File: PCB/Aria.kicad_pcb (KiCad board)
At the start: 4 copper layers, 30 x 85 mm, 85 parts, among them J1 B2B-PH-K-S(LF)(SN), J2 B3B-PH-K-S(LF)(SN), J3 20021121-00010C4LF, J4 0475890001-MicroUSBPort, P1 CONN_01X20, P2 CONN_01X20, Q1 DMG2307L-7, Q2 DMG2307L-7, SW1 B3U-1000P, SW2 B3U-1000P, T1 1909763-1, U1 BQ24210DQCT, U2 AZ1117CR-3.3TRG1_1, U3 STM32F446RET6_-_TQFP64, U4 ESP8285, X1 ABM3B8.000MHZB2T, X2 ABS07-32.768KHZ-9-T, X3 FA-128_26.0000MF10Z-AC3

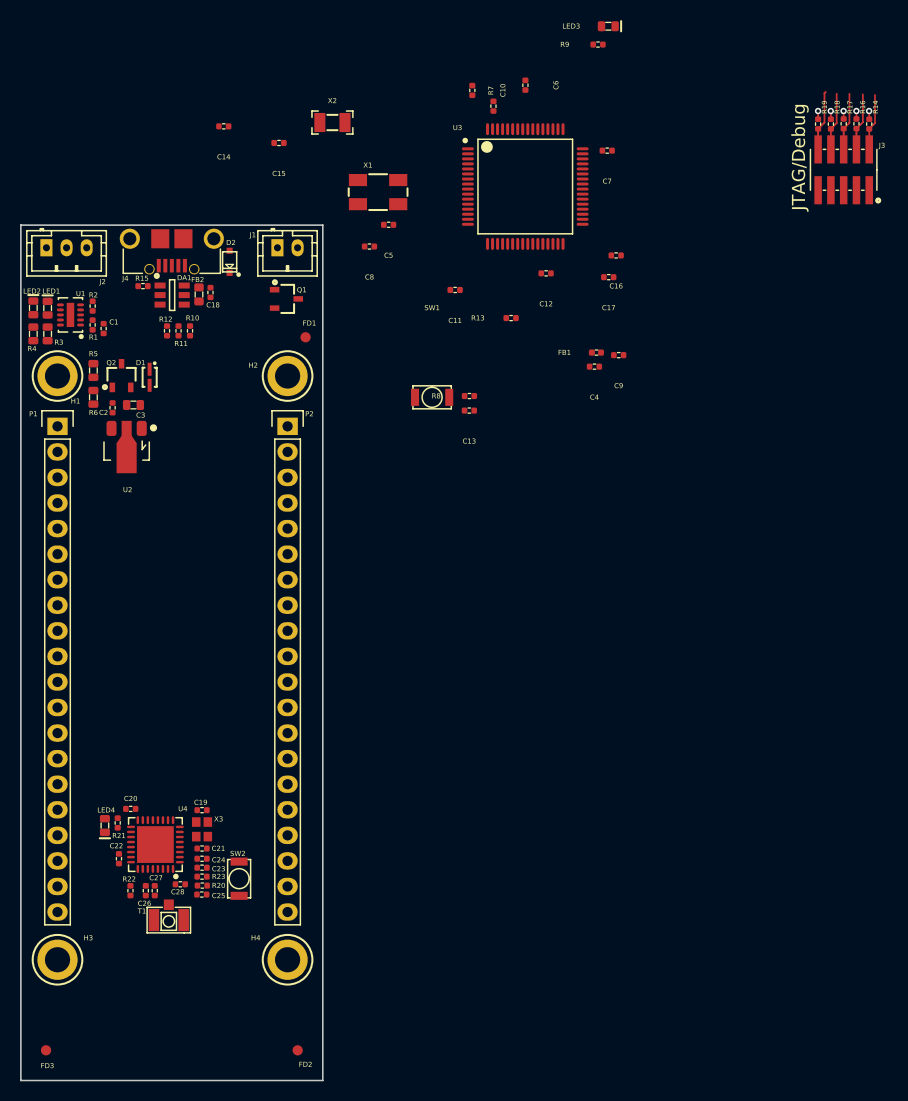
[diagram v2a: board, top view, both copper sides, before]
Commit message: Finished Placement and Mapping
Components placed, some routing completed. pin header mapping figured
out.
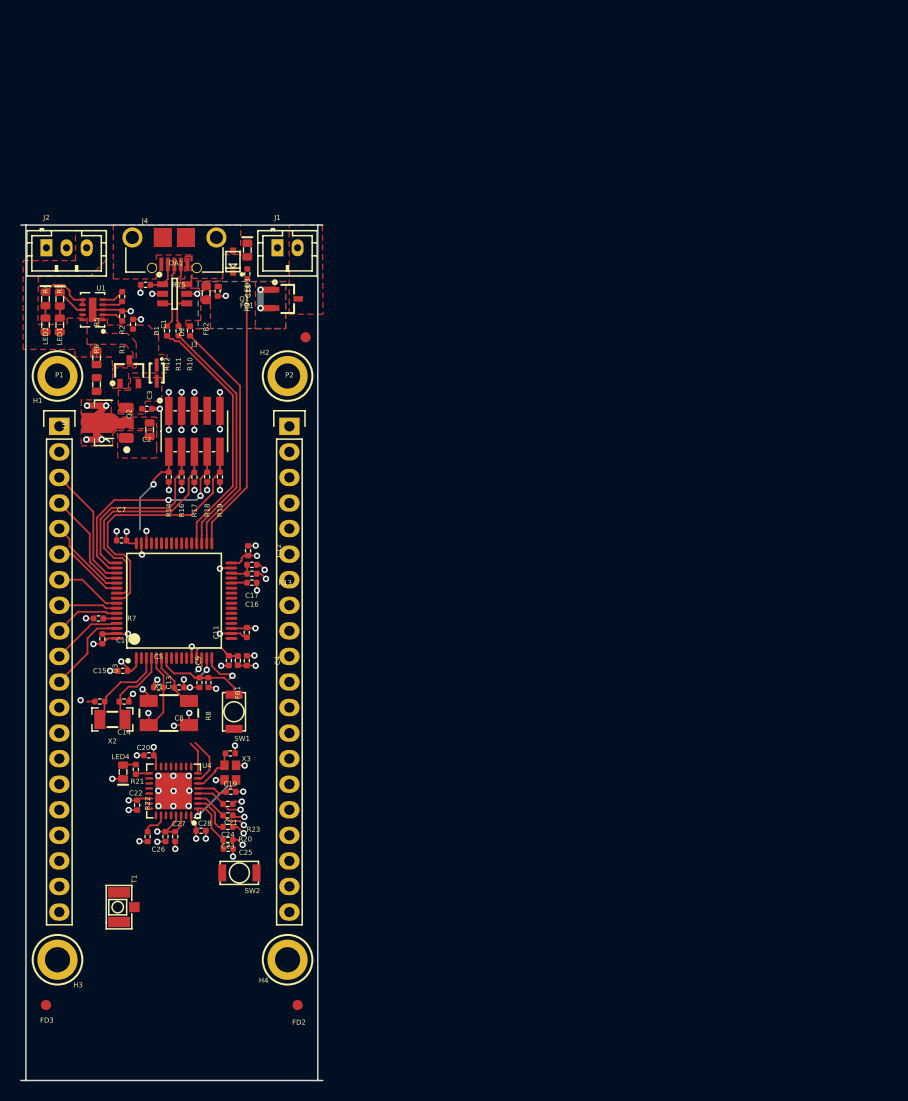
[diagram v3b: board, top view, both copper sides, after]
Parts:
- moved R14 77.9 mm to (68.2, 55.0), turned to 90 degrees
- moved R16 75.7 mm to (69.5, 55.1), turned to 90 degrees
- moved R17 73.5 mm to (70.7, 55.1), turned to 90 degrees
- moved R18 71.2 mm to (72.0, 55.0), turned to 90 degrees
- moved J3 69.5 mm to (70.7, 50.5), turned to 180 degrees
- moved C6 69.2 mm to (61.6, 71.1)
- moved R19 69.0 mm to (73.3, 55.0), turned to 90 degrees
- moved C10 67.3 mm to (63.6, 74.3), turned to 180 degrees
- moved R7 64.3 mm to (61.2, 69.1), turned to 180 degrees
- moved X2 63.2 mm to (62.6, 79.1), turned to 180 degrees
- moved C7 61.9 mm to (63.5, 61.3), turned to 180 degrees
- moved C15 58.3 mm to (61.3, 77.3), turned to 180 degrees
- moved C14 58.0 mm to (63.8, 77.3)
- moved X1 55.8 mm to (68.2, 78.5)
- moved U3 54.0 mm to (68.7, 67.3), turned to 90 degrees
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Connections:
- net Net-(U3-Pad20) renamed /MCU_STM32F446RET6/PA4
- C1 pad 1: /Power/VBUS -> /MCU_STM32F446RET6/VBUS
- C25 pad 1: /WiFi-ESP8285/STM_ESP_RST -> /MCU_STM32F446RET6/STM_ESP_RST
- D1 pad 1: /Power/VBUS -> /MCU_STM32F446RET6/VBUS
- P1 pad 10: Net-(P1-Pad10) -> /MCU_STM32F446RET6/PB8
- P1 pad 11: Net-(P1-Pad11) -> /MCU_STM32F446RET6/PB9
- P1 pad 12: Net-(P1-Pad12) -> /MCU_STM32F446RET6/PC0
- P1 pad 13: Net-(P1-Pad13) -> /MCU_STM32F446RET6/PC1
- P1 pad 14: Net-(P1-Pad14) -> /MCU_STM32F446RET6/PC3
- P1 pad 15: Net-(P1-Pad15) -> /MCU_STM32F446RET6/PC13
- P1 pad 16: Net-(P1-Pad16) -> /MCU_STM32F446RET6/PB0
- P1 pad 17: Net-(P1-Pad17) -> /MCU_STM32F446RET6/PB1
- P1 pad 18: Net-(P1-Pad18) -> GND
- P1 pad 19: Net-(P1-Pad19) -> +3V3
- P1 pad 3: Net-(P1-Pad3) -> /MCU_STM32F446RET6/PC10
- P1 pad 4: Net-(P1-Pad4) -> /MCU_STM32F446RET6/PC11
- P1 pad 5: Net-(P1-Pad5) -> /MCU_STM32F446RET6/PC12
- P1 pad 6: Net-(P1-Pad6) -> /MCU_STM32F446RET6/ESPTOST_BOOT0
- P1 pad 7: Net-(P1-Pad7) -> /MCU_STM32F446RET6/PB5
- P1 pad 8: Net-(P1-Pad8) -> /MCU_STM32F446RET6/PB6
- P1 pad 9: Net-(P1-Pad9) -> /MCU_STM32F446RET6/PB7
- P2 pad 10: Net-(P2-Pad10) -> /MCU_STM32F446RET6/PC6
- P2 pad 11: Net-(P2-Pad11) -> /MCU_STM32F446RET6/PC7
- P2 pad 12: Net-(P2-Pad12) -> /MCU_STM32F446RET6/PB10
- P2 pad 13: Net-(P2-Pad13) -> /MCU_STM32F446RET6/PC5
- P2 pad 14: Net-(P2-Pad14) -> /MCU_STM32F446RET6/PC4
- P2 pad 15: Net-(P2-Pad15) -> /MCU_STM32F446RET6/PA7
- P2 pad 16: Net-(P2-Pad16) -> /MCU_STM32F446RET6/PA6
- P2 pad 17: Net-(P2-Pad17) -> /MCU_STM32F446RET6/PA5
- P2 pad 18: Net-(P2-Pad18) -> GND
- P2 pad 19: Net-(P2-Pad19) -> +3V3
- P2 pad 3: Net-(P2-Pad3) -> /MCU_STM32F446RET6/PA8
- P2 pad 4: Net-(P2-Pad4) -> /MCU_STM32F446RET6/PA9
- P2 pad 5: Net-(P2-Pad5) -> /MCU_STM32F446RET6/PA10
- P2 pad 6: Net-(P2-Pad6) -> /MCU_STM32F446RET6/PA11
- P2 pad 7: Net-(P2-Pad7) -> /MCU_STM32F446RET6/PA12
- P2 pad 8: Net-(P2-Pad8) -> /MCU_STM32F446RET6/PC8
- P2 pad 9: Net-(P2-Pad9) -> /MCU_STM32F446RET6/PC9
- Q1 pad 1: /Power/VBUS -> /MCU_STM32F446RET6/VBUS
- Q1 pad 2: /Power/VBUS -> /MCU_STM32F446RET6/VBUS
- Q2 pad 1: /Power/VBUS -> /MCU_STM32F446RET6/VBUS
- R20 pad 1: /WiFi-ESP8285/STM_ESP_RST -> /MCU_STM32F446RET6/STM_ESP_RST
- R5 pad 2: /Power/BAT_VOLT -> /MCU_STM32F446RET6/BAT_VOLT
- R6 pad 1: /Power/BAT_VOLT -> /MCU_STM32F446RET6/BAT_VOLT
- R7 pad 1: /MCU_STM32F446RET6/ESPTOST_BOOT0 -> Net-(R7-Pad1)
- SW1 pad 1: /MCU_STM32F446RET6/ESP_ST_RST -> Net-(SW1-Pad1)
- SW2 pad 2: /WiFi-ESP8285/STM_ESP_RST -> /MCU_STM32F446RET6/STM_ESP_RST
- U1 pad 1: /Power/VBUS -> /MCU_STM32F446RET6/VBUS
- U3 pad 11: Net-(U3-Pad11) -> /MCU_STM32F446RET6/PC3
- U3 pad 14: Net-(U3-Pad14) -> /MCU_STM32F446RET6/ESP_URX
- U3 pad 15: Net-(U3-Pad15) -> /MCU_STM32F446RET6/ESP_UTX
- U3 pad 16: Net-(U3-Pad16) -> /MCU_STM32F446RET6/STM_ESP_RST
- U3 pad 17: Net-(U3-Pad17) -> /MCU_STM32F446RET6/ESP_PGM_MODE
- U3 pad 2: Net-(U3-Pad2) -> /MCU_STM32F446RET6/PC13
- U3 pad 21: Net-(U3-Pad21) -> /MCU_STM32F446RET6/PA5
- U3 pad 22: Net-(U3-Pad22) -> /MCU_STM32F446RET6/PA6
- U3 pad 23: Net-(U3-Pad23) -> /MCU_STM32F446RET6/PA7
- U3 pad 24: Net-(U3-Pad24) -> /MCU_STM32F446RET6/PC4
- U3 pad 25: Net-(U3-Pad25) -> /MCU_STM32F446RET6/PC5
- U3 pad 26: Net-(U3-Pad26) -> /MCU_STM32F446RET6/PB0
- U3 pad 27: Net-(U3-Pad27) -> /MCU_STM32F446RET6/PB1
- U3 pad 29: Net-(U3-Pad29) -> /MCU_STM32F446RET6/PB10
- U3 pad 37: Net-(U3-Pad37) -> /MCU_STM32F446RET6/PC6
- U3 pad 38: Net-(U3-Pad38) -> /MCU_STM32F446RET6/PC7
- U3 pad 39: Net-(U3-Pad39) -> /MCU_STM32F446RET6/PC8
- U3 pad 40: Net-(U3-Pad40) -> /MCU_STM32F446RET6/PC9
- U3 pad 41: Net-(U3-Pad41) -> /MCU_STM32F446RET6/PA8
- U3 pad 42: Net-(U3-Pad42) -> /MCU_STM32F446RET6/PA9
- U3 pad 43: Net-(U3-Pad43) -> /MCU_STM32F446RET6/PA10
- U3 pad 44: Net-(U3-Pad44) -> /MCU_STM32F446RET6/PA11
- U3 pad 45: Net-(U3-Pad45) -> /MCU_STM32F446RET6/PA12
- U3 pad 51: /MCU_STM32F446RET6/ESP_UTX -> /MCU_STM32F446RET6/PC10
- U3 pad 52: /MCU_STM32F446RET6/ESP_URX -> /MCU_STM32F446RET6/PC11
- U3 pad 53: /MCU_STM32F446RET6/STM_ESP_RST -> /MCU_STM32F446RET6/PC12
- U3 pad 54: /MCU_STM32F446RET6/ESP_PGM_MODE -> /MCU_STM32F446RET6/ESPTOST_BOOT0
- U3 pad 57: Net-(U3-Pad57) -> /MCU_STM32F446RET6/PB5
- U3 pad 58: Net-(U3-Pad58) -> /MCU_STM32F446RET6/PB6
- U3 pad 59: Net-(U3-Pad59) -> /MCU_STM32F446RET6/PB7
- U3 pad 60: /MCU_STM32F446RET6/ESPTOST_BOOT0 -> Net-(R7-Pad1)
- U3 pad 61: Net-(U3-Pad61) -> /MCU_STM32F446RET6/PB8
- U3 pad 62: Net-(U3-Pad62) -> /MCU_STM32F446RET6/PB9
- U3 pad 8: Net-(U3-Pad8) -> /MCU_STM32F446RET6/PC0
- U3 pad 9: Net-(U3-Pad9) -> /MCU_STM32F446RET6/PC1
- U4 pad 22: /WiFi-ESP8285/ESPTOST_BOOT1 -> /MCU_STM32F446RET6/ESPTOST_BOOT1
- U4 pad 23: /WiFi-ESP8285/ESPTOST_BOOT0 -> /MCU_STM32F446RET6/ESPTOST_BOOT0
- U4 pad 24: /WiFi-ESP8285/ESP_ST_RST -> /MCU_STM32F446RET6/ESP_ST_RST
- U4 pad 25: /WiFi-ESP8285/ESP_UTX -> /MCU_STM32F446RET6/ESP_UTX
- U4 pad 26: /WiFi-ESP8285/ESP_URX -> /MCU_STM32F446RET6/ESP_URX
- U4 pad 32: /WiFi-ESP8285/STM_ESP_RST -> /MCU_STM32F446RET6/STM_ESP_RST
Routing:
- net GND: track 0.00 -> 92.4 mm, vias 0 -> 56
- net +3V3: track 4.03 -> 57.0 mm, vias 5 -> 27
- net /MCU_STM32F446RET6/HEARTBEAT: track 0.00 -> 27.8 mm
- net Net-(R12-Pad1): track 0.00 -> 25.2 mm
- net Net-(R11-Pad1): track 0.00 -> 24.4 mm
- net Net-(R10-Pad1): track 0.00 -> 24.1 mm
- net /MCU_STM32F446RET6/NJTRST: track 6.03 -> 26.0 mm
- net /MCU_STM32F446RET6/SWO_TDO: track 5.76 -> 23.4 mm
- net /MCU_STM32F446RET6/SWO_TDI: track 5.76 -> 22.2 mm, vias 0 -> 2
- net /MCU_STM32F446RET6/STM_ESP_RST: track 0.00 -> 14.2 mm, vias 0 -> 2
- net /MCU_STM32F446RET6/SWCLK_TCK: track 5.73 -> 18.9 mm
- net /MCU_STM32F446RET6/PC10: track 0.00 -> 12.6 mm
- net /MCU_STM32F446RET6/PC11: track 0.00 -> 10.6 mm
- net /MCU_STM32F446RET6/ESP_ST_RST: track 0.00 -> 9.27 mm
- net /MCU_STM32F446RET6/PB9: track 0.00 -> 8.98 mm
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- added copper zone on F.Cu, net +3V3
- added copper zone on F.Cu, net /Power/BAT
- added copper zone on B.Cu, net /Power/VBUS
- added copper zone on F.Cu, net /Power/VBUS
- added copper zone on F.Cu, net GND
- added copper zone on F.Cu, net Net-(C18-Pad2)
- added copper zone on F.Cu, net Net-(C2-Pad1)
- added copper zone on F.Cu, net Net-(D2-Pad1)
- added copper zone on F.Cu, net Net-(J1-Pad2)
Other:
- outline, holes or cut-outs redrawn
- board text removed: "JTAG/Debug"

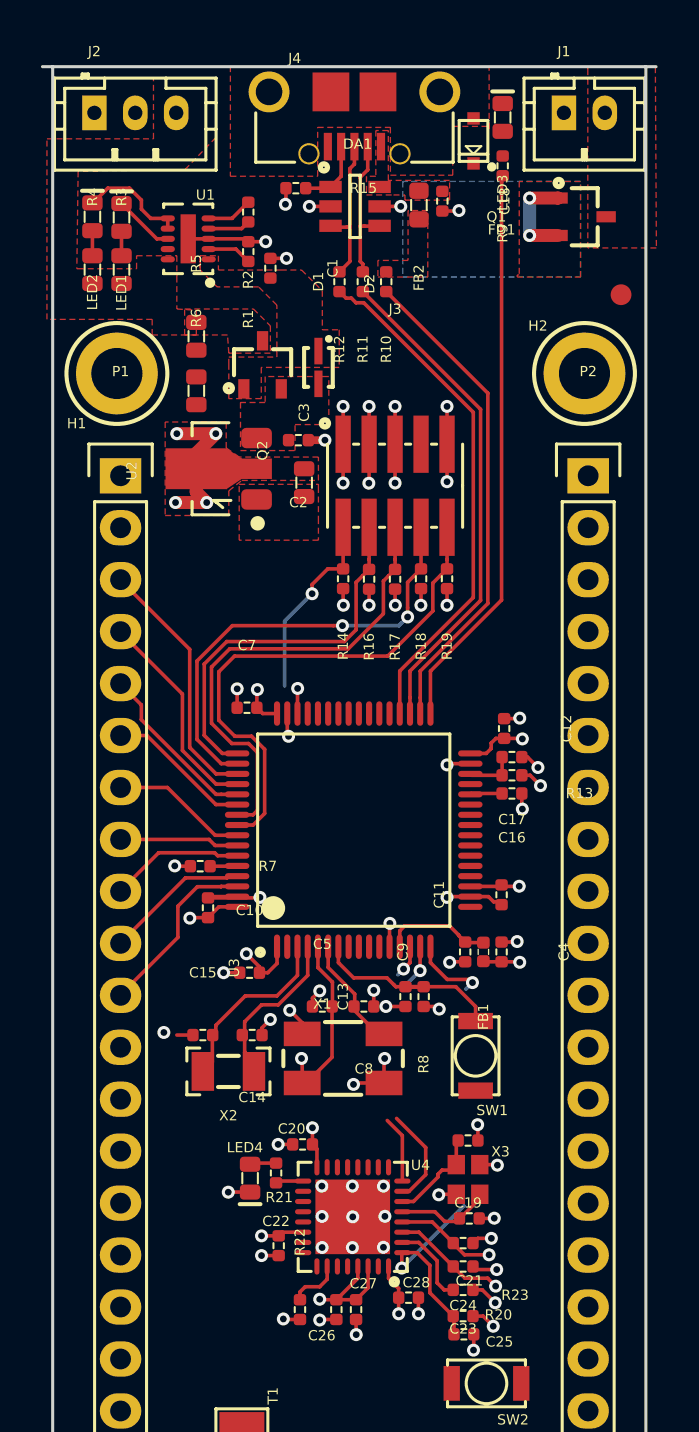
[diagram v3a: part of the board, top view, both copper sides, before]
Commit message: Layout
layout underway, one side completely routed, next other side, ESP, and
PCB antenna. Added PDF for app not on 2.4GHZ antenna similar to the one
sparkfun uses in their thing boards, I suspect this is where they got it
and it seems reliable.
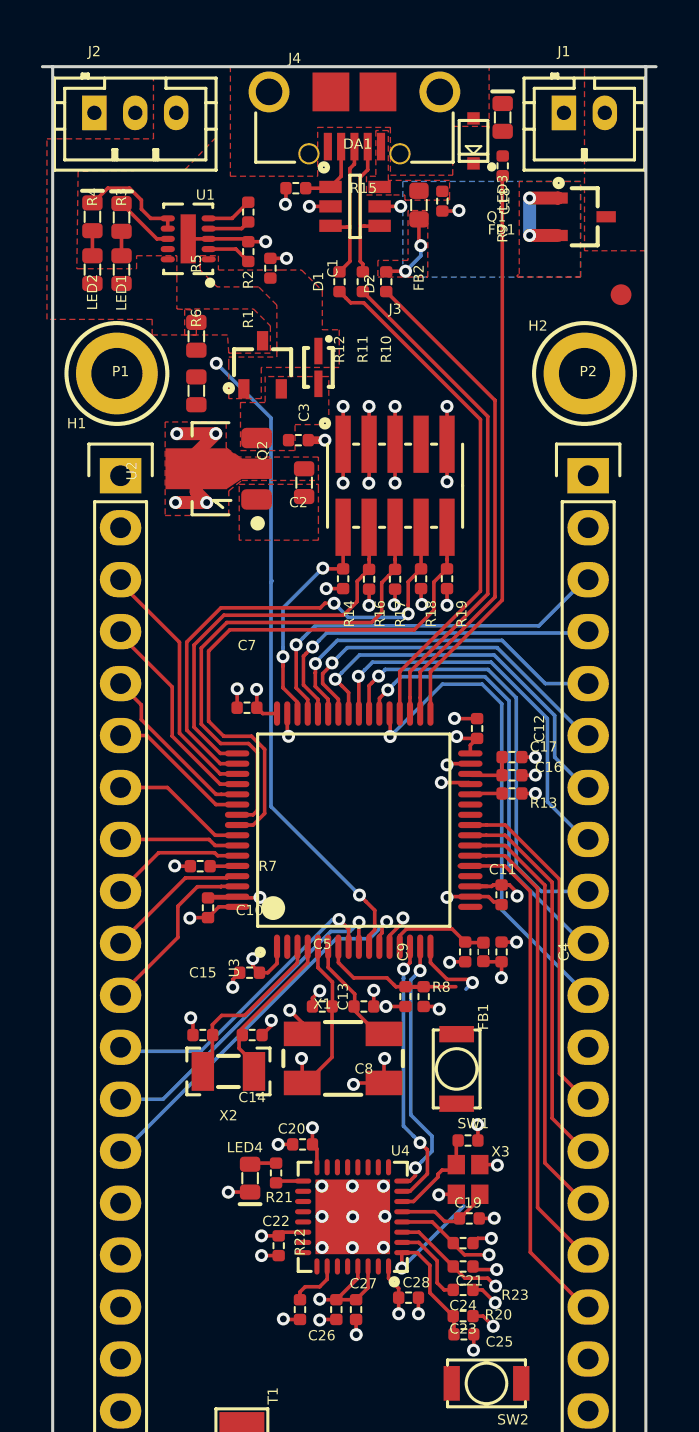
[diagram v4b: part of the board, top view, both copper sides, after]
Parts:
- moved C12 1.32 mm to (74.8, 62.4)
- moved SW1 1.13 mm to (73.8, 79.0)
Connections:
- P2 pad 10: /MCU_STM32F446RET6/PC6 -> /MCU_STM32F446RET6/PC7
- P2 pad 11: /MCU_STM32F446RET6/PC7 -> /MCU_STM32F446RET6/PC6
- P2 pad 3: /MCU_STM32F446RET6/PA8 -> /MCU_STM32F446RET6/PA12
- P2 pad 4: /MCU_STM32F446RET6/PA9 -> /MCU_STM32F446RET6/PA11
- P2 pad 6: /MCU_STM32F446RET6/PA11 -> /MCU_STM32F446RET6/PA9
- P2 pad 7: /MCU_STM32F446RET6/PA12 -> /MCU_STM32F446RET6/PA8
- P2 pad 8: /MCU_STM32F446RET6/PC8 -> /MCU_STM32F446RET6/PC9
- P2 pad 9: /MCU_STM32F446RET6/PC9 -> /MCU_STM32F446RET6/PC8
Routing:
- net /MCU_STM32F446RET6/BAT_VOLT: track 0.00 -> 31.9 mm, vias 0 -> 2
- net /MCU_STM32F446RET6/PA5: track 0.00 -> 25.6 mm
- net /MCU_STM32F446RET6/PC6: track 0.00 -> 24.1 mm, vias 0 -> 1
- net /MCU_STM32F446RET6/PA6: track 0.00 -> 23.0 mm
- net /MCU_STM32F446RET6/PC8: track 0.00 -> 21.7 mm, vias 0 -> 1
- net /MCU_STM32F446RET6/PC7: track 0.00 -> 21.6 mm, vias 0 -> 1
- net /MCU_STM32F446RET6/PA7: track 0.00 -> 21.0 mm
- net /MCU_STM32F446RET6/PC9: track 0.00 -> 19.3 mm, vias 0 -> 1
- net /MCU_STM32F446RET6/PA12: track 0.00 -> 19.2 mm, vias 0 -> 1
- net /MCU_STM32F446RET6/PC3: track 0.00 -> 19.0 mm, vias 0 -> 1
- net /MCU_STM32F446RET6/PC4: track 0.00 -> 18.9 mm
- net /MCU_STM32F446RET6/PA8: track 0.00 -> 18.7 mm, vias 0 -> 1
- net /MCU_STM32F446RET6/PA9: track 0.00 -> 17.6 mm, vias 0 -> 1
- net /MCU_STM32F446RET6/PA11: track 0.00 -> 17.5 mm, vias 0 -> 1
- net /MCU_STM32F446RET6/PA10: track 0.00 -> 17.4 mm, vias 0 -> 1
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
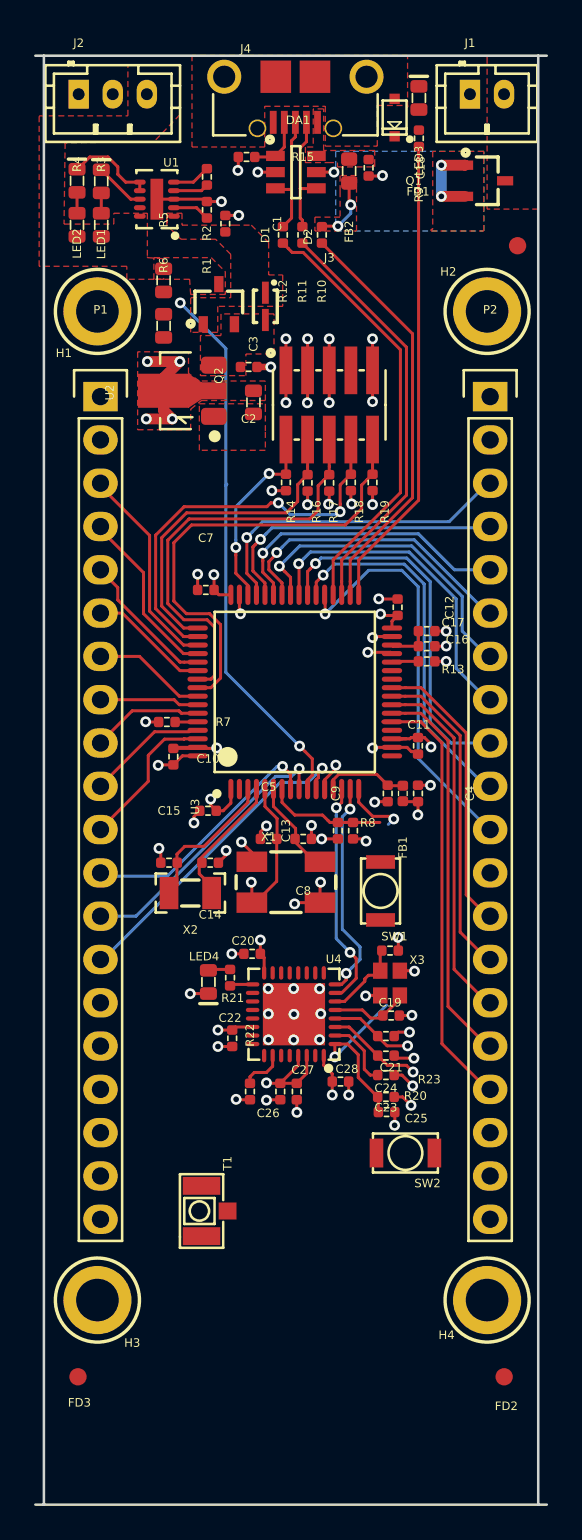
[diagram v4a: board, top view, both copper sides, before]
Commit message: Board Size. Routing and Antenna
Board Size tweaked. More signals routed. Next will be pin swapping and
routing finished. Also experimented with importing a PCB antenna design
from bitmap, still can't get it quite right, hopefully nex commit.
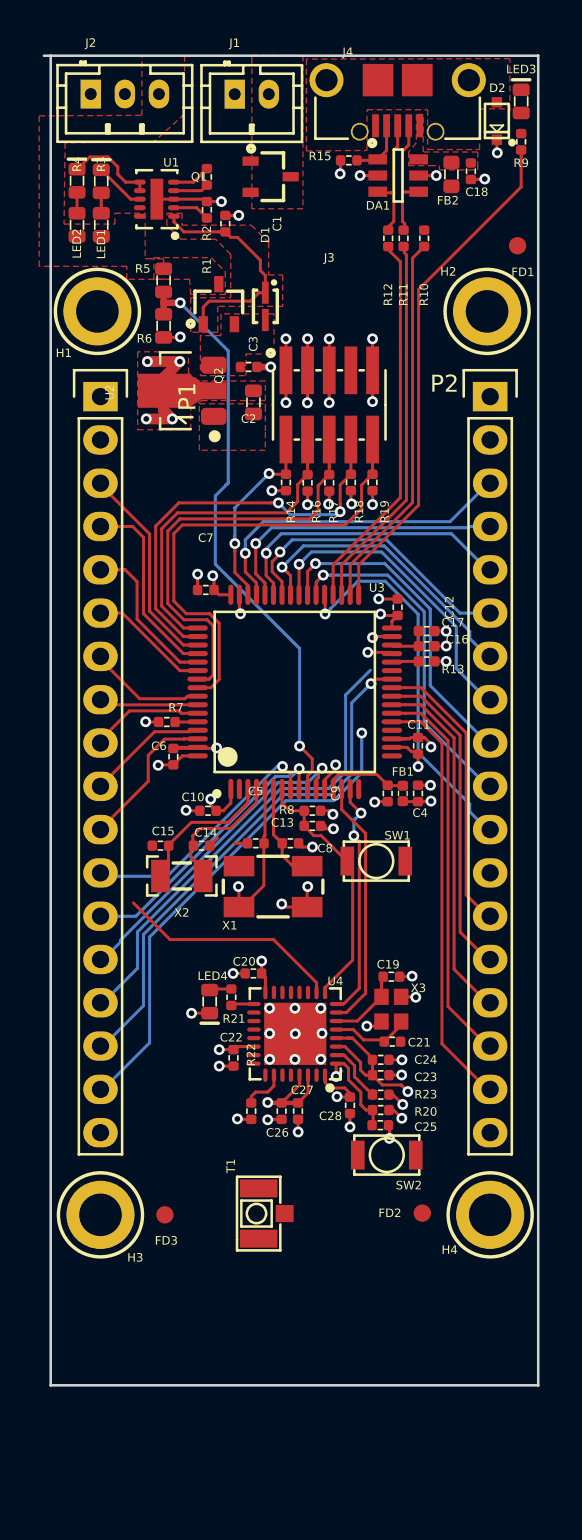
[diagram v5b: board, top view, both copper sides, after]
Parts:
- P1, P2: value CONN_01X20 -> CONN_01X18; footprint Pin_Headers:Pin_Header_Straight_1x20 -> Socket_Strips:Socket_Strip_Straight_1x18
- moved J1 13.8 mm to (65.2, 32.3)
- moved Q1 12.6 mm to (67.3, 37.1)
- moved FD3 10.8 mm to (61.1, 98.0)
- moved FD2 10.7 mm to (76.2, 97.9)
- moved R12 6.18 mm to (74.2, 40.7)
- moved C18 6.00 mm to (79.1, 36.8)
- moved D2 6.00 mm to (80.6, 33.8)
- moved DA1 6.00 mm to (74.8, 37.0)
- moved FB2 6.00 mm to (77.9, 37.0)
- moved J4 6.00 mm to (74.8, 34.1)
- moved LED3 6.00 mm to (82.0, 32.7)
- moved R10 6.00 mm to (76.3, 40.7)
- moved R15 6.00 mm to (71.9, 36.1)
- moved R9 6.00 mm to (82.0, 35.0)
- moved R11 5.94 mm to (75.1, 40.7)
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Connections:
- net Net-(T1-Pad1) renamed /WiFi-ESP8285/ANTENNA
- SW1 pad 1: Net-(SW1-Pad1) -> /MCU_STM32F446RET6/ESP_ST_RST
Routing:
- net /MCU_STM32F446RET6/PB0: track 0.00 -> 31.0 mm, vias 0 -> 1
- net /MCU_STM32F446RET6/PB1: track 0.00 -> 29.0 mm, vias 0 -> 1
- net /MCU_STM32F446RET6/PC13: track 0.00 -> 27.8 mm
- net /MCU_STM32F446RET6/ESPTOST_BOOT0: track 7.28 -> 20.5 mm
- net /MCU_STM32F446RET6/STM_ESP_RST: track 14.2 -> 6.19 mm, vias 2 -> 1
- net /MCU_STM32F446RET6/ESP_ST_RST: track 7.90 -> 14.8 mm
- net /MCU_STM32F446RET6/VBUS: track 8.45 -> 13.4 mm, vias 4 -> 0
- net GND: track 92.6 -> 89.3 mm, vias 57 -> 54
- net Net-(R12-Pad1): track 25.5 -> 22.6 mm
- net /MCU_STM32F446RET6/BAT_VOLT: track 31.9 -> 34.8 mm
- net Net-(R11-Pad1): track 24.7 -> 22.1 mm
- net /MCU_STM32F446RET6/PC8: track 21.7 -> 19.3 mm
- net /MCU_STM32F446RET6/HEARTBEAT: track 27.8 -> 30.1 mm
- net Net-(R10-Pad1): track 24.3 -> 22.2 mm
- net /MCU_STM32F446RET6/PC7: track 21.6 -> 20.1 mm
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- removed copper zone on B.Cu, net /Power/VBUS
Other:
- board size 30 x 85 mm -> 29 x 78 mm
